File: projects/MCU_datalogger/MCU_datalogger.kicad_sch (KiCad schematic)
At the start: 25 parts, among them U1 24LC1025, U2 DS1337S_, U3 24LC1025, U4 ATMEGA328P-AU, Y1 32.768KHz, Y2 16MHz

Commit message: MCU datalogger schematic - fix bug in SCL and SCK clock signals
Rename SCK net label to SCL where appropriate in both schematic
drawings (Root and Connectors) to fix bug where pins 17 and 28
of the ATMEGA were incorrectly shorted because of a confusion of
two clock different signals:
- SCK for ICSP
- SCL for I2C
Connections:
- net SCK: no longer R2.2, U1.6 (SCL), U2.6 (SCL), U3.6 (SCL), U4.28 (PC5)
- new net SCL: R2.2, U1.6 (SCL), U2.6 (SCL), U3.6 (SCL), U4.28 (PC5)
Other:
- sheet Connectors ports: added SCL; removed none
- note added: "GPIO"
- note added: "I2C"
- note added: "ICSP"
- note added: "UART"

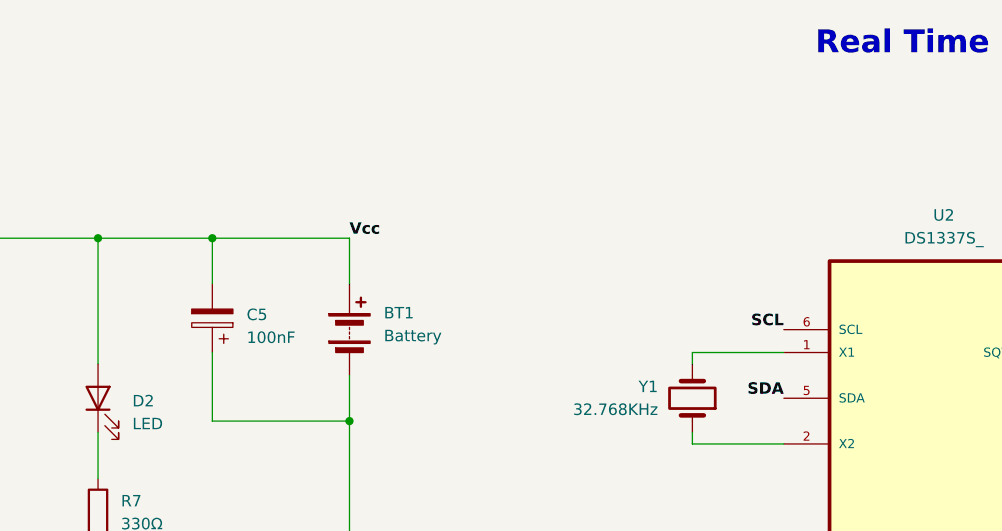
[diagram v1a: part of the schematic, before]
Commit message: MCU datalogger - add BOM, modify polarized cap, add datasheets
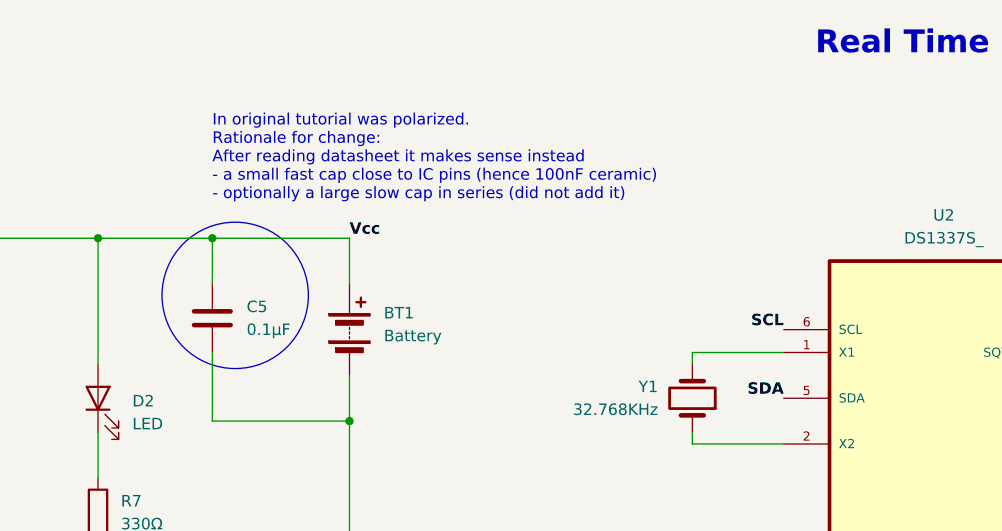
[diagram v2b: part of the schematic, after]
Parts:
- BT1: now left out of the parts list
- C5: value 100nF -> 0.1μF; symbol Device:C_Polarized -> Device:C
- U1, U3: LCSC# (none) -> C183301
- U2: LCSC# (none) -> C9867
- U4: LCSC# (none) -> aliexpress
- Y1: LCSC# (none) -> C32346
- Y2: LCSC# (none) -> C112572
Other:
- note added: "In original tutorial was polarized. Rationale for change: After reading datasheet it makes sense instead - a small fast cap close to IC pins (hence 100nF ceramic) - optionally a large slow cap in series (did not add it)"
